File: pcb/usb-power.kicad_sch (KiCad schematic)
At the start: 9 parts, among them J2 USB4110-GF-A, U9 AP2112K-3.3

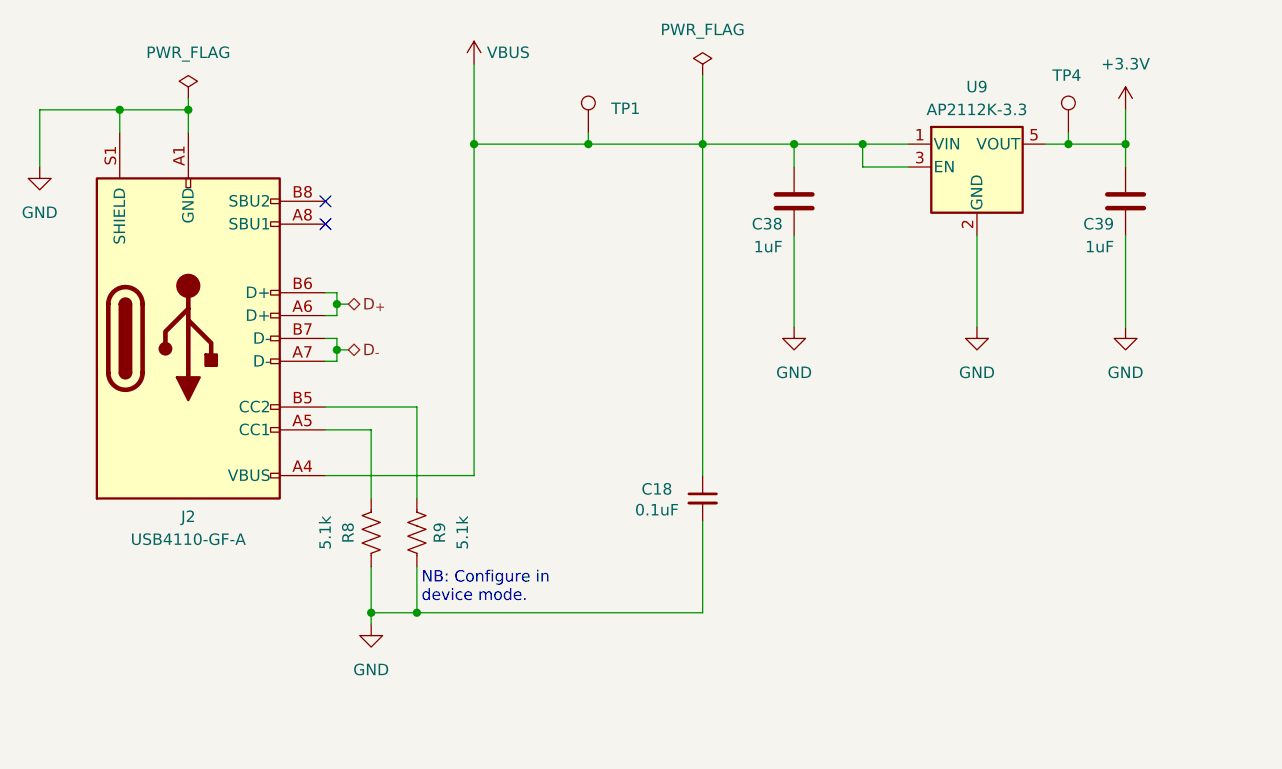
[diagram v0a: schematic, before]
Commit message: Add USB diode protection (#35)
- Change revision g -> h
  - schematic
  - pcb
  - silk screen
* Add 3d parts
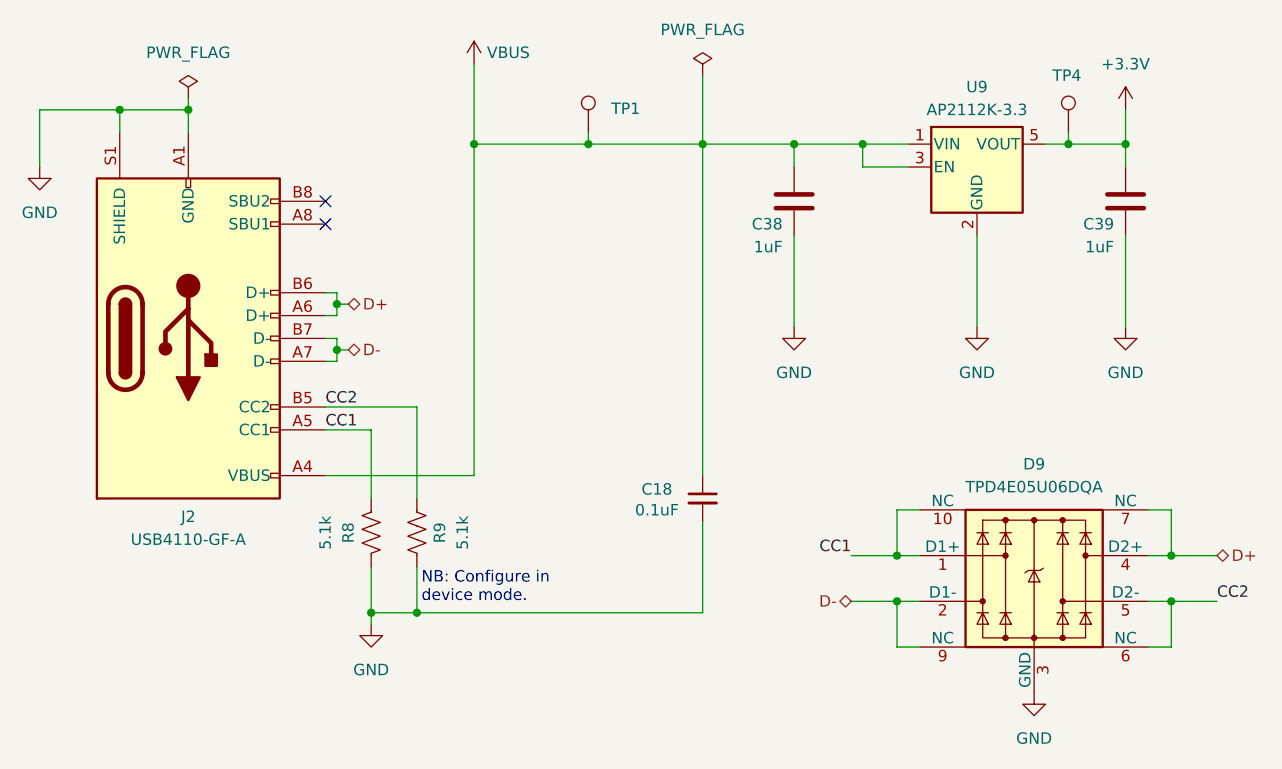
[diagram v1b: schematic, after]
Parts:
- added D9: TPD4E05U06DQA, Package_SON:USON-10_2.5x1.0mm_P0.5mm, symbol Power_Protection:TPD4E05U06DQA
- J2: footprint Connector_USB:USB_C_Receptacle_GCT_USB4110 -> open-ephys:USB_C_Receptacle_GCT_USB4110
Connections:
- net GND: now also D9.3 (GND), D9.8 (GND)
- net CC2: now reaches J2.B5 (CC2), R9.2
- net CC2: now also D9.5 (D2-), D9.6 (NC)
- net CC1: now reaches J2.A5 (CC1), R8.2
- net CC1: now also D9.1 (D1+), D9.10 (NC)
- net D_{+} renamed D+
- net D+: now also D9.4 (D2+), D9.7 (NC)
- net D_{-} renamed D-
- net D-: now also D9.2 (D1-), D9.9 (NC)
